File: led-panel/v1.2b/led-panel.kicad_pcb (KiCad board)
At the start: 2 copper layers, 34 x 40 mm, 25 parts, among them J1 5V, J2 PMOD, J3 jmp, J4 PMOD, J5 jmp, J6 Conn_02x08_Odd_Even, J7 jmp, U1 SN74LVC8T245, U2 SN74LVC8T245

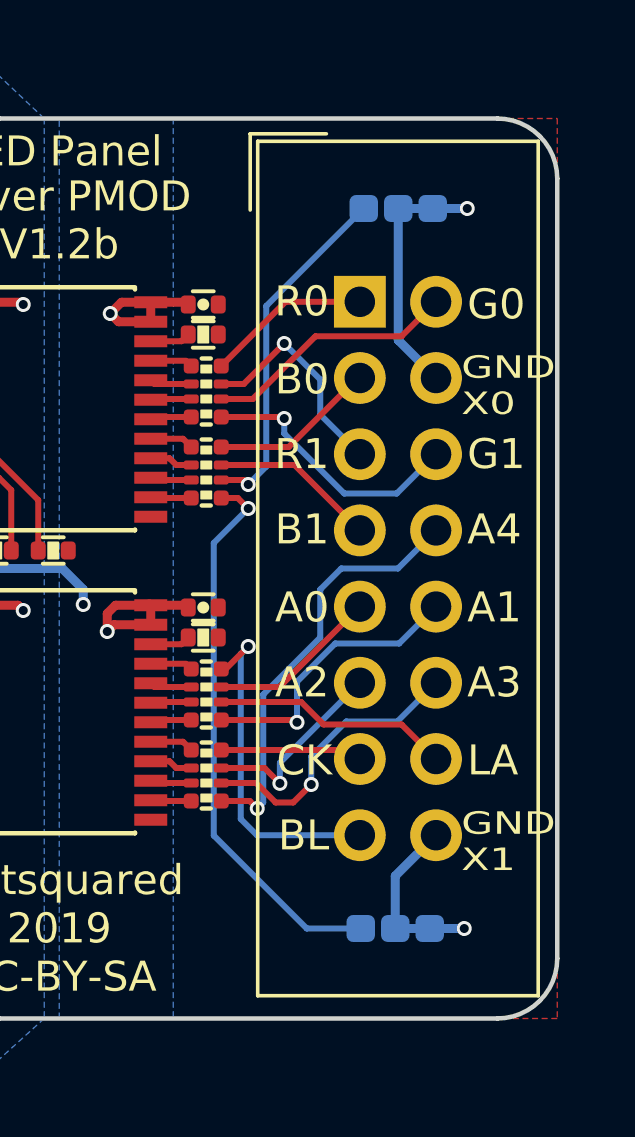
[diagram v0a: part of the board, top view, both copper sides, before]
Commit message: Corrected led panel pmod project name.
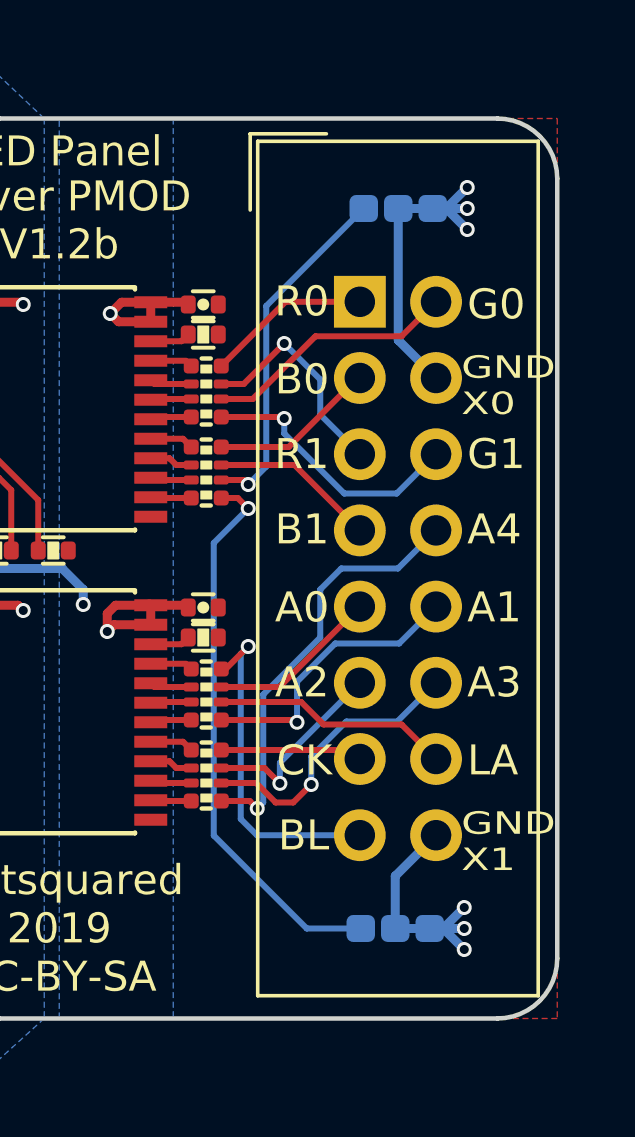
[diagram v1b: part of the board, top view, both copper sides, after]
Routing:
- net GND: track 4.23 -> 9.09 mm, vias 2 -> 6
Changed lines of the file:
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@@
     (thickness 0.8)
     (drawings 150)
-    (tracks 261)
+    (tracks 272)
     (zones 0)
     (modules 25)
@@
   (page A4)
   (title_block
-    (title "iCEBreaker PMOD - Hyperram")
+    (title "iCEBreaker PMOD - LED Panel HUB75E")
     (rev V1.2b)
     (company 1BitSquared)
@@
   )
   (setup
-    (last_trace_width 0.3)
+    (last_trace_width 0.2)
     (user_trace_width 0.3)
     (trace_clearance 0.2)
@@
   (via (at 68.3 56) (size 0.5) (drill 0.3) (layers F.Cu B.Cu) (net 1))
   (segment (start 67.15 56) (end 68.3 56) (width 0.3) (layer B.Cu) (net 1))
+  (segment (start 67.15 56) (end 67.6 56) (width 0.3) (layer B.Cu) (net 1))
+  (via (at 68.3 56.7) (size 0.5) (drill 0.3) (layers F.Cu B.Cu) (net 1))
+  (segment (start 67.6 56) (end 68.3 56.7) (width 0.3) (layer B.Cu) (net 1))
+  (via (at 68.3 55.300006) (size 0.5) (drill 0.3) (layers F.Cu B.Cu) (net 1))
+  (segment (start 68.299994 55.300006) (end 68.3 55.300006) (width 0.3) (layer B.Cu) (net 1))
+  (segment (start 67.6 56) (end 68.299994 55.300006) (width 0.3) (layer B.Cu) (net 1))
+  (segment (start 67.25 32) (end 67.7 32) (width 0.3) (layer B.Cu) (net 1))
+  (via (at 68.4 32.7) (size 0.5) (drill 0.3) (layers F.Cu B.Cu) (net 1))
+  (segment (start 67.7 32) (end 68.4 32.7) (width 0.3) (layer B.Cu) (net 1))
+  (via (at 68.4 31.3) (size 0.5) (drill 0.3) (layers F.Cu B.Cu) (net 1))
+  (segment (start 67.7 32) (end 68.4 31.3) (width 0.3) (layer B.Cu) (net 1))
   (segment (start 44 38.92) (end 47.1 42.02) (width 0.3) (layer B.Cu) (net 2))
   (segment (start 47.1 42.02) (end 47.1 42.85) (width 0.3) (layer B.Cu) (net 2))

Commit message: Some global cleanup.
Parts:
- added REF**: null_Logo_SilkS_5mm, pkl_logos:null_Logo_SilkS_5mm, B.Cu at (58.0, 44.2)
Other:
- board size 34 x 40 mm -> 34 x 39 mm
- board text added: "NULL"
